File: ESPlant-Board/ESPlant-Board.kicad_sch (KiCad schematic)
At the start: 30 parts, among them J1 Conn_01x05, U1 ESP32-S2-MINI-1-N4, U3 Reset, U4 Boot, U5 Temp/Humid-Sensor, U6 Light sensor, U7 AMS1117-3_3, U8 MK-12C02-G025

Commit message: board, case: more work
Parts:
- U8: JLCPCB Position Offset (none) -> 0,0,-0.5
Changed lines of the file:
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@@
+      (effects (font (size 1.27 1.27)) hide)
+    )
+    (property "JLCPCB Position Offset" "" (at 101.6 109.22 0)
       (effects (font (size 1.27 1.27)) hide)
     )
@@
       (effects (font (size 1.27 1.27)) hide)
     )
+    (property "JLCPCB Position Offset" "" (at 146.05 143.51 0)
+      (effects (font (size 1.27 1.27)) hide)
+    )
     (pin "1")
     (pin "2")
@@
     )
     (property "MPN" "C2297" (at 140.97 90.17 0)
+      (effects (font (size 1.27 1.27)) hide)
+    )
+    (property "JLCPCB Position Offset" "" (at 140.97 90.17 0)
       (effects (font (size 1.27 1.27)) hide)
     )
@@
       (effects (font (size 1.27 1.27)) hide)
     )
+    (property "JLCPCB Position Offset" "" (at 92.71 109.22 0)
+      (effects (font (size 1.27 1.27)) hide)
+    )
     (pin "1")
     (pin "2")
@@
       (effects (font (size 1.27 1.27)) hide)
     )
+    (property "JLCPCB Position Offset" "" (at 229.87 33.02 0)
+      (effects (font (size 1.27 1.27)) hide)
+    )
     (pin "1")
     (pin "2")
@@
       (effects (font (size 1.27 1.27)) hide)
     )
+    (property "JLCPCB Position Offset" "" (at 87.63 109.22 0)
+      (effects (font (size 1.27 1.27)) hide)
+    )
     (pin "1")
     (pin "2")
@@
       (effects (font (size 1.27 1.27)) hide)
     )
+    (property "JLCPCB Position Offset" "" (at 242.57 33.02 0)
+      (effects (font (size 1.27 1.27)) hide)
+    )
     (pin "1")
     (pin "2")
@@
       (effects (font (size 1.27 1.27)) hide)
     )
+    (property "JLCPCB Position Offset" "" (at 146.05 138.43 0)
+      (effects (font (size 1.27 1.27)) hide)
+    )
     (pin "1")
     (pin "2")
@@
       (effects (font (size 1.27 1.27)) hide)
     )
+    (property "JLCPCB Position Offset" "" (at 91.44 97.79 0)
+      (effects (font (size 1.27 1.27)) hide)
+    )
     (pin "1")
     (pin "2")
@@
       (effects (font (size 1.27 1.27)) hide)
     )
+    (property "JLCPCB Position Offset" "" (at 255.27 74.93 0)
+      (effects (font (size 1.27 1.27)) hide)
+    )
     (pin "1")
     (pin "2")
@@
     )
     (property "MPN" "C25905" (at 55.88 142.24 0)
+      (effects (font (size 1.27 1.27)) hide)
+    )
+    (property "JLCPCB Position Offset" "" (at 55.88 142.24 0)
       (effects (font (size 1.27 1.27)) hide)
     )
@@
       (effects (font (size 1.27 1.27)) hide)
     )
-    (pin "1")
-    (pin "10")
+    (property "JLCPCB Position Offset" "" (at 193.04 97.79 0)
+      (effects (font (size 1.27 1.27)) hide)
+    )
+    (pin "1")
     (pin "12")
     (pin "16")
@@
     (pin "3")
     (pin "30")
-    (pin "36")
     (pin "42")
     (pin "43")
@@
     (pin "64")
     (pin "65")
+    (pin "10")
     (pin "11")
     (pin "13")
@@
     (pin "34")
     (pin "35")
+    (pin "36")
     (pin "37")
     (pin "38")
@@
       (effects (font (size 1.27 1.27)) hide)
     )
+    (property "JLCPCB Position Offset" "" (at 100.33 177.8 0)
+      (effects (font (size 1.27 1.27)) hide)
+    )
     (pin "1")
     (pin "2")
@@
       (effects (font (size 1.27 1.27)) hide)
     )
+    (property "JLCPCB Position Offset" "" (at 212.09 109.22 0)
+      (effects (font (size 1.27 1.27)) hide)
+    )
     (pin "1")
     (pin "2")
@@
     )
     (property "MPN" "C778186" (at 111.76 146.05 0)
+      (effects (font (size 1.27 1.27)) hide)
+    )
+    (property "JLCPCB Position Offset" "0,0,-0.5" (at 111.76 146.05 0)
       (effects (font (size 1.27 1.27)) hide)
     )
@@
       (effects (font (size 1.27 1.27)) hide)
     )
+    (property "JLCPCB Position Offset" "" (at 64.77 40.64 0)
+      (effects (font (size 1.27 1.27)) hide)
+    )
     (pin "1")
     (pin "2")
@@
     )
     (property "JLCPCB Rotation Offset" "" (at 58.42 34.29 0)
+      (effects (font (size 1.27 1.27)) hide)
+    )
+    (property "JLCPCB Position Offset" "" (at 58.42 34.29 0)
       (effects (font (size 1.27 1.27)) hide)
     )
@@
     )
     (property "MPN" "C2827328" (at 45.72 135.89 0)
+      (effects (font (size 1.27 1.27)) hide)
+    )
+    (property "JLCPCB Position Offset" "" (at 45.72 135.89 0)
       (effects (font (size 1.27 1.27)) hide)
     )
@@
       (effects (font (size 1.27 1.27)) hide)
     )
+    (property "JLCPCB Position Offset" "" (at 106.68 109.22 0)
+      (effects (font (size 1.27 1.27)) hide)
+    )
     (pin "1")
     (pin "2")
@@
       (effects (font (size 1.27 1.27)) hide)
     )
+    (property "JLCPCB Position Offset" "" (at 46.99 64.77 0)
+      (effects (font (size 1.27 1.27)) hide)
+    )
     (pin "1")
     (pin "2")
@@
     )
     (property "MPN" "C10418" (at 64.77 176.53 0)
+      (effects (font (size 1.27 1.27)) hide)
+    )
+    (property "JLCPCB Position Offset" "" (at 64.77 176.53 0)
       (effects (font (size 1.27 1.27)) hide)
     )
@@
       (effects (font (size 1.27 1.27)) hide)
     )
+    (property "JLCPCB Position Offset" "" (at 247.65 63.5 0)
+      (effects (font (size 1.27 1.27)) hide)
+    )
     (pin "1")
     (pin "1")
@@
       (effects (font (size 1.27 1.27)) hide)
     )
+    (property "JLCPCB Position Offset" "" (at 247.65 93.98 0)
+      (effects (font (size 1.27 1.27)) hide)
+    )
     (pin "1")
     (pin "1")
@@
       (effects (font (size 1.27 1.27)) hide)
     )
+    (property "JLCPCB Position Offset" "" (at 140.97 100.33 0)
+      (effects (font (size 1.27 1.27)) hide)
+    )
     (pin "1")
     (pin "2")
@@
     )
     (property "MPN" "C25905" (at 35.56 142.24 0)
+      (effects (font (size 1.27 1.27)) hide)
+    )
+    (property "JLCPCB Position Offset" "" (at 35.56 142.24 0)
       (effects (font (size 1.27 1.27)) hide)
     )
@@
       (effects (font (size 1.27 1.27)) hide)
     )
+    (property "JLCPCB Position Offset" "" (at 255.27 105.41 0)
+      (effects (font (size 1.27 1.27)) hide)
+    )
     (pin "1")
     (pin "2")
@@
     )
     (property "MPN" "C94599" (at 33.02 160.02 0)
+      (effects (font (size 1.27 1.27)) hide)
+    )
+    (property "JLCPCB Position Offset" "" (at 33.02 160.02 0)
       (effects (font (size 1.27 1.27)) hide)
     )
@@
       (effects (font (size 1.27 1.27)) hide)
     )
+    (property "JLCPCB Position Offset" "" (at 250.19 138.43 0)
+      (effects (font (size 1.27 1.27)) hide)
+    )
     (pin "1")
     (pin "2")
@@
       (effects (font (size 1.27 1.27)) hide)
     )
+    (property "JLCPCB Position Offset" "" (at 133.35 176.53 0)
+      (effects (font (size 1.27 1.27)) hide)
+    )
     (pin "1")
     (pin "2")
@@
       (effects (font (size 1.27 1.27)) hide)
     )
+    (property "JLCPCB Position Offset" "" (at 64.77 71.12 0)
+      (effects (font (size 1.27 1.27)) hide)
+    )

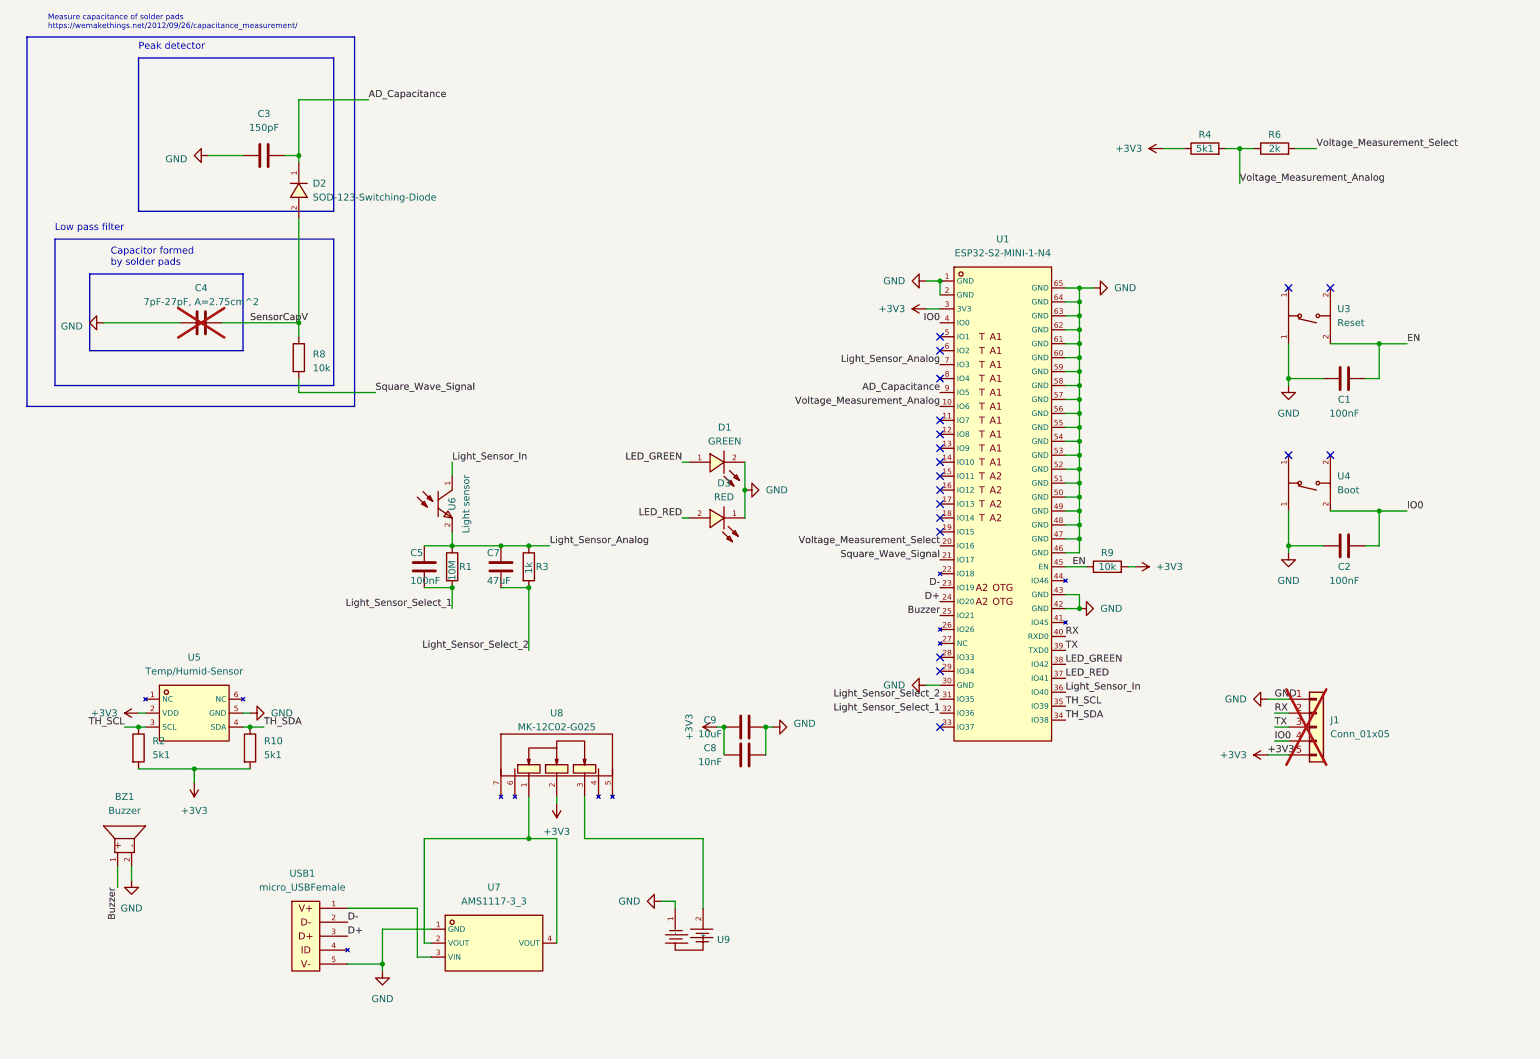
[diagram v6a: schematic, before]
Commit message: Board: changed to esp32-c6-mini-1-n4
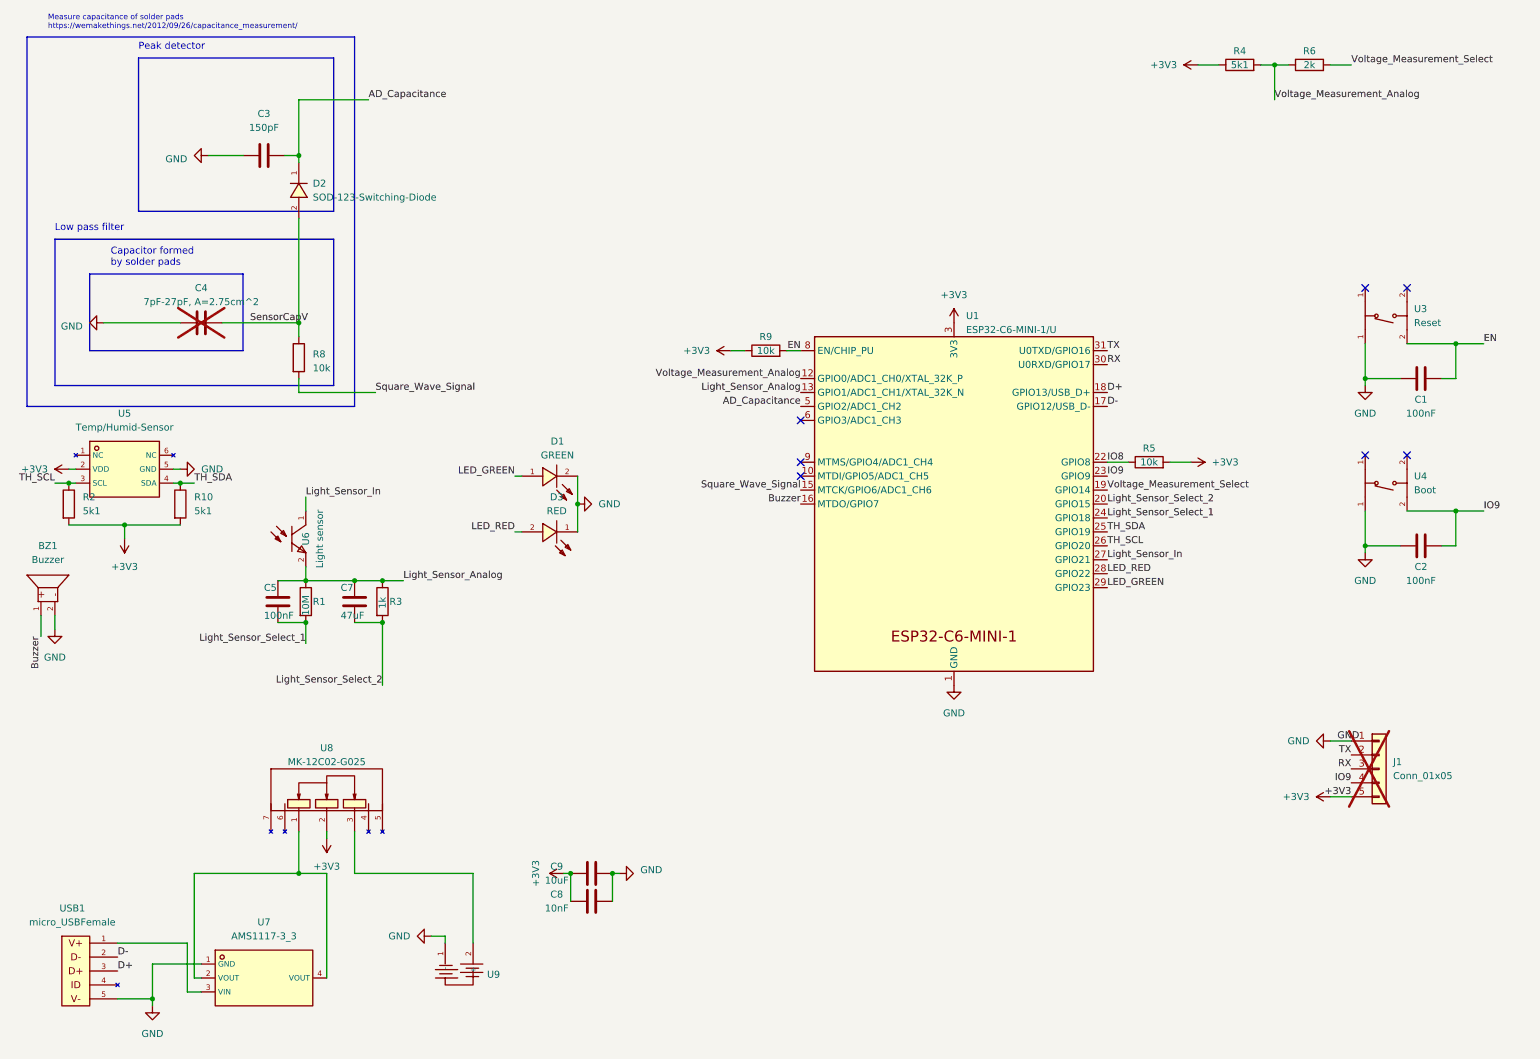
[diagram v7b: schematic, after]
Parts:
- removed U1: ESP32-S2-MINI-1-N4, CustomFootprints:WIFI-SMD_ESP32-MINI-1-N4, symbol Custom_Parts:ESP32-S2-MINI-1-N4
- added R5: 10k, Resistor_SMD:R_0402_1005Metric, symbol Device:R
- added U1: ESP32-C6-MINI-1/U, Espressif:ESP32-C6-MINI-1, symbol Espressif:ESP32-C6-MINI-1/U
- C4, J1, U9: LCSC (none) -> /; MPN (none) -> /
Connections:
- net IO0 is gone; now on net IO9: C2.2, J1.4 (Pin_4), U4.2 (D)
- net +3V3: now also R9.1, R5.2, U1.3 (3V3); no longer R9.2
- net AD_Capacitance: now also U1.5 (GPIO2/ADC1_CH2)
- net Buzzer: now also U1.16 (MTDO/GPIO7)
- net D+: now also U1.18 (GPIO13/USB_D+)
- net D-: now also U1.17 (GPIO12/USB_D-)
- net EN: now also R9.2, U1.8 (EN/CHIP_PU); no longer R9.1
- net GND: now also U1.1 (GND), U1.11 (GND), U1.14 (GND), U1.2 (GND), U1.36 (GND), U1.37 (GND), U1.38 (GND), U1.39 (GND), U1.40 (GND), U1.41 (GND), U1.42 (GND), U1.43 (GND), U1.44 (GND), U1.45 (GND), U1.46 (GND), U1.47 (GND), U1.48 (GND), U1.49 (GND), U1.50 (GND), U1.51 (GND), U1.52 (GND), U1.53 (GND)
- net LED_GREEN: now also U1.29 (GPIO23)
- net LED_RED: now also U1.28 (GPIO22)
- net Light_Sensor_Analog: now also U1.13 (GPIO1/ADC1_CH1/XTAL_32K_N)
- net Light_Sensor_In: now also U1.27 (GPIO21)
- net Light_Sensor_Select_1: now also U1.24 (GPIO18)
- net Light_Sensor_Select_2: now also U1.20 (GPIO15)
- net RX: now also J1.3 (Pin_3), U1.30 (U0RXD/GPIO17); no longer J1.2 (Pin_2)
- net Square_Wave_Signal: now also U1.15 (MTCK/GPIO6/ADC1_CH6)
- net TH_SCL: now also U1.26 (GPIO20)
- net TH_SDA: now also U1.25 (GPIO19)
- net TX: now also J1.2 (Pin_2), U1.31 (U0TXD/GPIO16); no longer J1.3 (Pin_3)
- net Voltage_Measurement_Analog: now also U1.12 (GPIO0/ADC1_CH0/XTAL_32K_P)
- net Voltage_Measurement_Select: now also U1.19 (GPIO14)
- net IO9: now reaches U4.2 (D)
- net IO9: now also U1.23 (GPIO9)
- new net IO8: R5.1, U1.22 (GPIO8)
- no-connect marks 19 -> 7
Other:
- moved on the sheet: BZ1, C1, C2, C5, C7, C8, C9, D1, D3, R1, R10, R2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
